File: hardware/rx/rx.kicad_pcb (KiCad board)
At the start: 2 copper layers, 23.9 x 37 mm, 16 parts, among them J1 Conn_01x04, J3 PPM, J4 AUX2, J6 VIN, SW1 SW_Push, U1 E28-2G4M12S, U3 ESP32-C3_SUPERMINI, U5 MIC5219-3.3YM5

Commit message: rx PCB
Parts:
- added J2: VBAT, unfancyRemote_components:SolderWirePad_1x01_SMD_1x2mm, F.Cu at (136.9, 65.2)
- added JP1: SolderJumper_2_Open, Jumper:SolderJumper-2_P1.3mm_Open_RoundedPad1.0x1.5mm, F.Cu at (135.9, 67.9)
- added JP2: SolderJumper_2_Open, Jumper:SolderJumper-2_P1.3mm_Open_RoundedPad1.0x1.5mm, F.Cu at (135.9, 73.1)
- added JP3: SolderJumper_2_Open, Jumper:SolderJumper-2_P1.3mm_Open_RoundedPad1.0x1.5mm, F.Cu at (135.9, 70.5)
- added JP4: SolderJumper_2_Open, Jumper:SolderJumper-2_P1.3mm_Open_RoundedPad1.0x1.5mm, F.Cu at (135.9, 75.7)
- added JP5: SolderJumper_2_Open, Jumper:SolderJumper-2_P1.3mm_Open_RoundedPad1.0x1.5mm, F.Cu at (135.9, 78.3)
- added JP6: SolderJumper_2_Open, Jumper:SolderJumper-2_P1.3mm_Open_RoundedPad1.0x1.5mm, F.Cu at (135.9, 80.9)
- added R10: 150K, Resistor_SMD:R_0402_1005Metric, F.Cu at (133.6, 80.6)
- added R11: 3.3K, Resistor_SMD:R_0402_1005Metric, F.Cu at (132.6, 80.6)
- added R2: 120K, Resistor_SMD:R_0402_1005Metric, F.Cu at (133.6, 72.8)
- added R3: 6.8K, Resistor_SMD:R_0402_1005Metric, F.Cu at (132.6, 72.8)
- added R4: 100K, Resistor_SMD:R_0402_1005Metric, F.Cu at (133.6, 70.2)
- added R5: 4.7K, Resistor_SMD:R_0402_1005Metric, F.Cu at (132.6, 70.2)
- added R6: 120K, Resistor_SMD:R_0402_1005Metric, F.Cu at (133.6, 75.4)
- added R7: 3.3K, Resistor_SMD:R_0402_1005Metric, F.Cu at (132.6, 75.4)
- added R8: 150K, Resistor_SMD:R_0402_1005Metric, F.Cu at (133.6, 78.0)
- added R9: 4.7K, Resistor_SMD:R_0402_1005Metric, F.Cu at (132.6, 78.0)
- R13: value 6.8K -> 5.6K
- moved SW1 15.3 mm to (134.0, 93.7)
- moved R12 8.64 mm to (133.6, 67.6), turned to -90 degrees
- moved R13 8.30 mm to (132.6, 67.6), turned to 90 degrees
- moved R1 3.90 mm to (127.9, 77.0)
- moved R14 3.90 mm to (127.9, 75.9)
- moved J4 1.60 mm to (143.5, 74.0)
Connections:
- R12 pad 1: VBAT -> 12S
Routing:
- net VBATSCALED: track 1.09 -> 43.9 mm
- net VBAT: track 0.00 -> 17.5 mm
- net Net-(R1-Pad1): track 9.79 -> 22.1 mm, vias 0 -> 2
- net +3V3: track 65.2 -> 75.4 mm, vias 4 -> 3
- net +5V: track 63.6 -> 72.9 mm
- net 22S: track 0.00 -> 1.94 mm
- net 18S: track 0.00 -> 1.94 mm
- net 14S: track 0.00 -> 1.94 mm
- net 20S: track 0.00 -> 1.94 mm
- net 16S: track 0.00 -> 1.94 mm
- net 12S: track 0.00 -> 1.93 mm
- net BSENSE: track 4.13 -> 3.04 mm
- net GND: vias 27 -> 38
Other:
- board text added: "12S"
- board text added: "14S"
- board text added: "16S"
- board text added: "18S"
- board text added: "20S"
- board text added: "22S"
- board text added: "PPM/VIN/-"
- board text added: "VBAT"

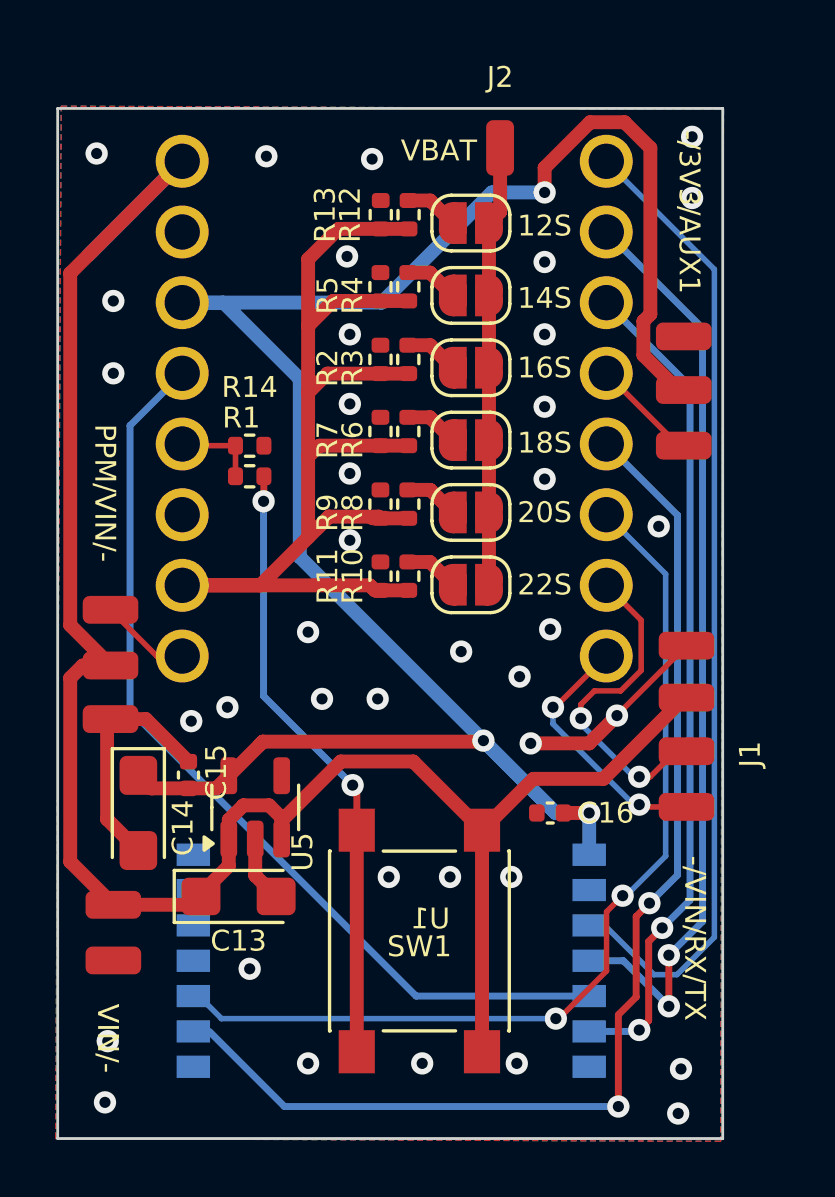
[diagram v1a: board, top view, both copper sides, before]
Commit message: update to kicad 9
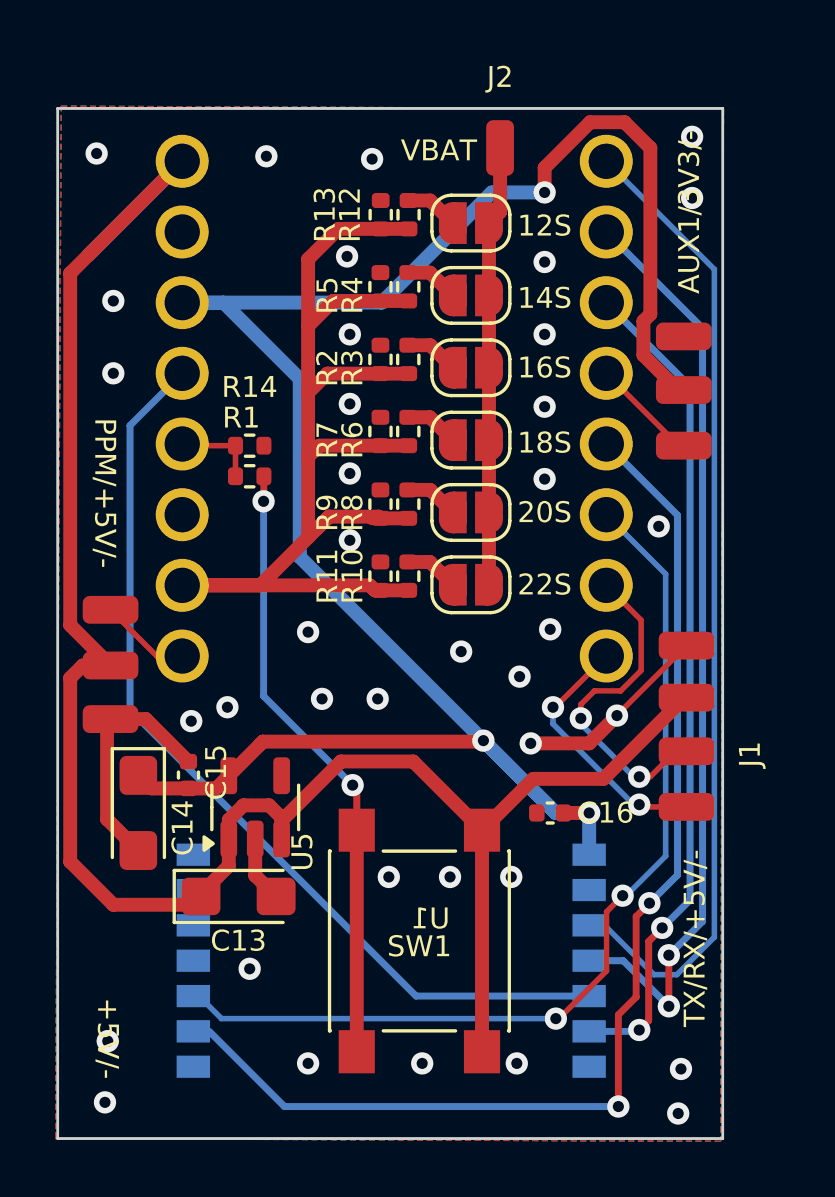
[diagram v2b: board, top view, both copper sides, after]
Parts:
- removed J6: VIN, unfancyRemote_components:SolderWirePad_1x02_SMD_1x2mm
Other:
- board text added: "+5V/-"
- board text added: "AUX1/3V3/-"
- board text added: "PPM/+5V/-"
- board text added: "TX/RX/+5V/-"
- board text removed: "-/3V3/AUX1"
- board text removed: "-/VIN/RX/TX"
- board text removed: "PPM/VIN/-"
- board text removed: "VIN/-"

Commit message: rx improvements
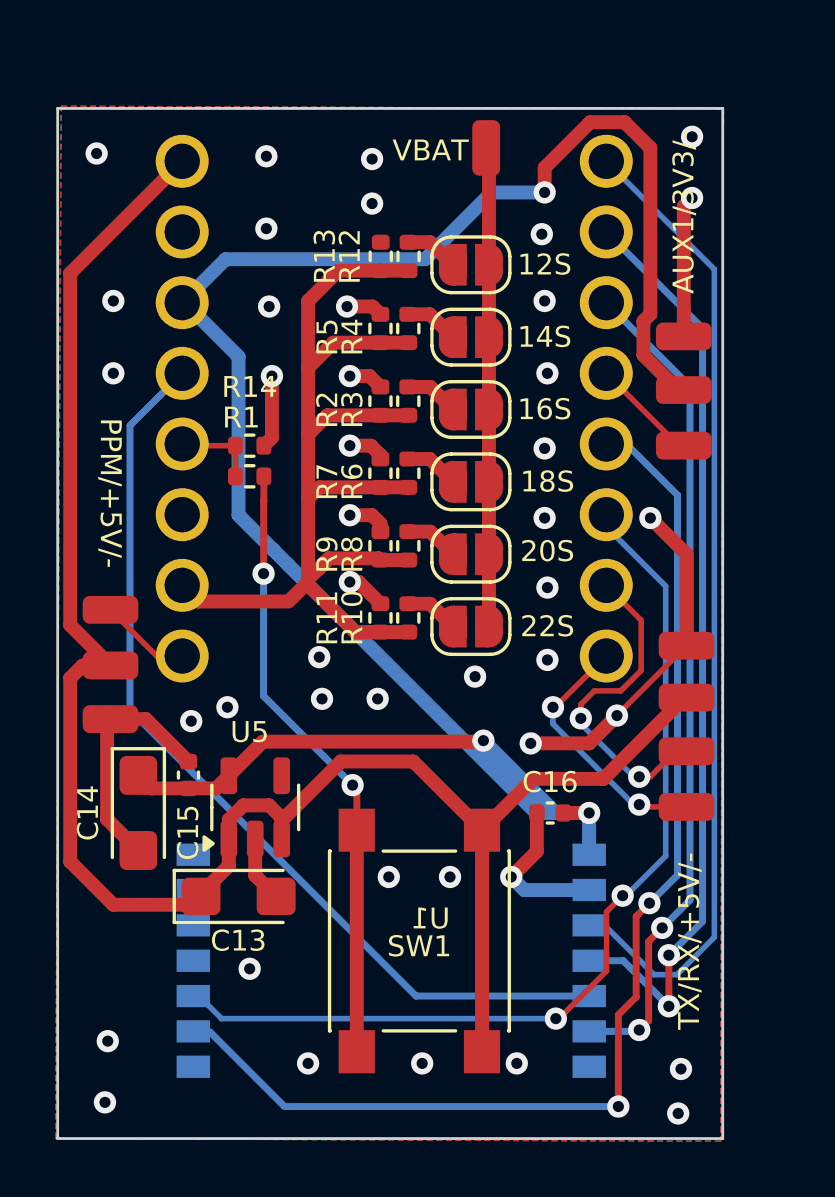
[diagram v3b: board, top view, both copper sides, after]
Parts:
- moved JP1 1.50 mm to (135.9, 69.4)
- moved JP2 1.50 mm to (135.9, 74.6)
- moved JP3 1.50 mm to (135.9, 72.0)
- moved JP4 1.50 mm to (135.9, 77.2)
- moved JP5 1.50 mm to (135.9, 79.8)
- moved JP6 1.50 mm to (135.9, 82.4)
- moved R10 1.50 mm to (133.6, 82.1)
- moved R11 1.50 mm to (132.6, 82.1)
- moved R12 1.50 mm to (133.6, 69.1)
- moved R13 1.50 mm to (132.6, 69.1)
- moved R2 1.50 mm to (133.6, 74.3)
- moved R3 1.50 mm to (132.6, 74.3)
- moved R4 1.50 mm to (133.6, 71.7)
- moved R5 1.50 mm to (132.6, 71.7)
- moved R6 1.50 mm to (133.6, 76.9)
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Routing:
- net GND: track 18.2 -> 43.6 mm, vias 38 -> 43
- net +5V: track 72.9 -> 67.2 mm
- net VBATSCALED: track 43.9 -> 39.9 mm
- net +3V3: track 75.4 -> 74.8 mm
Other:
- board text removed: "+5V/-"
